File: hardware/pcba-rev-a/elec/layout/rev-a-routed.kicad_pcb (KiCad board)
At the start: 2 copper layers, 200 x 146 mm, 180 parts

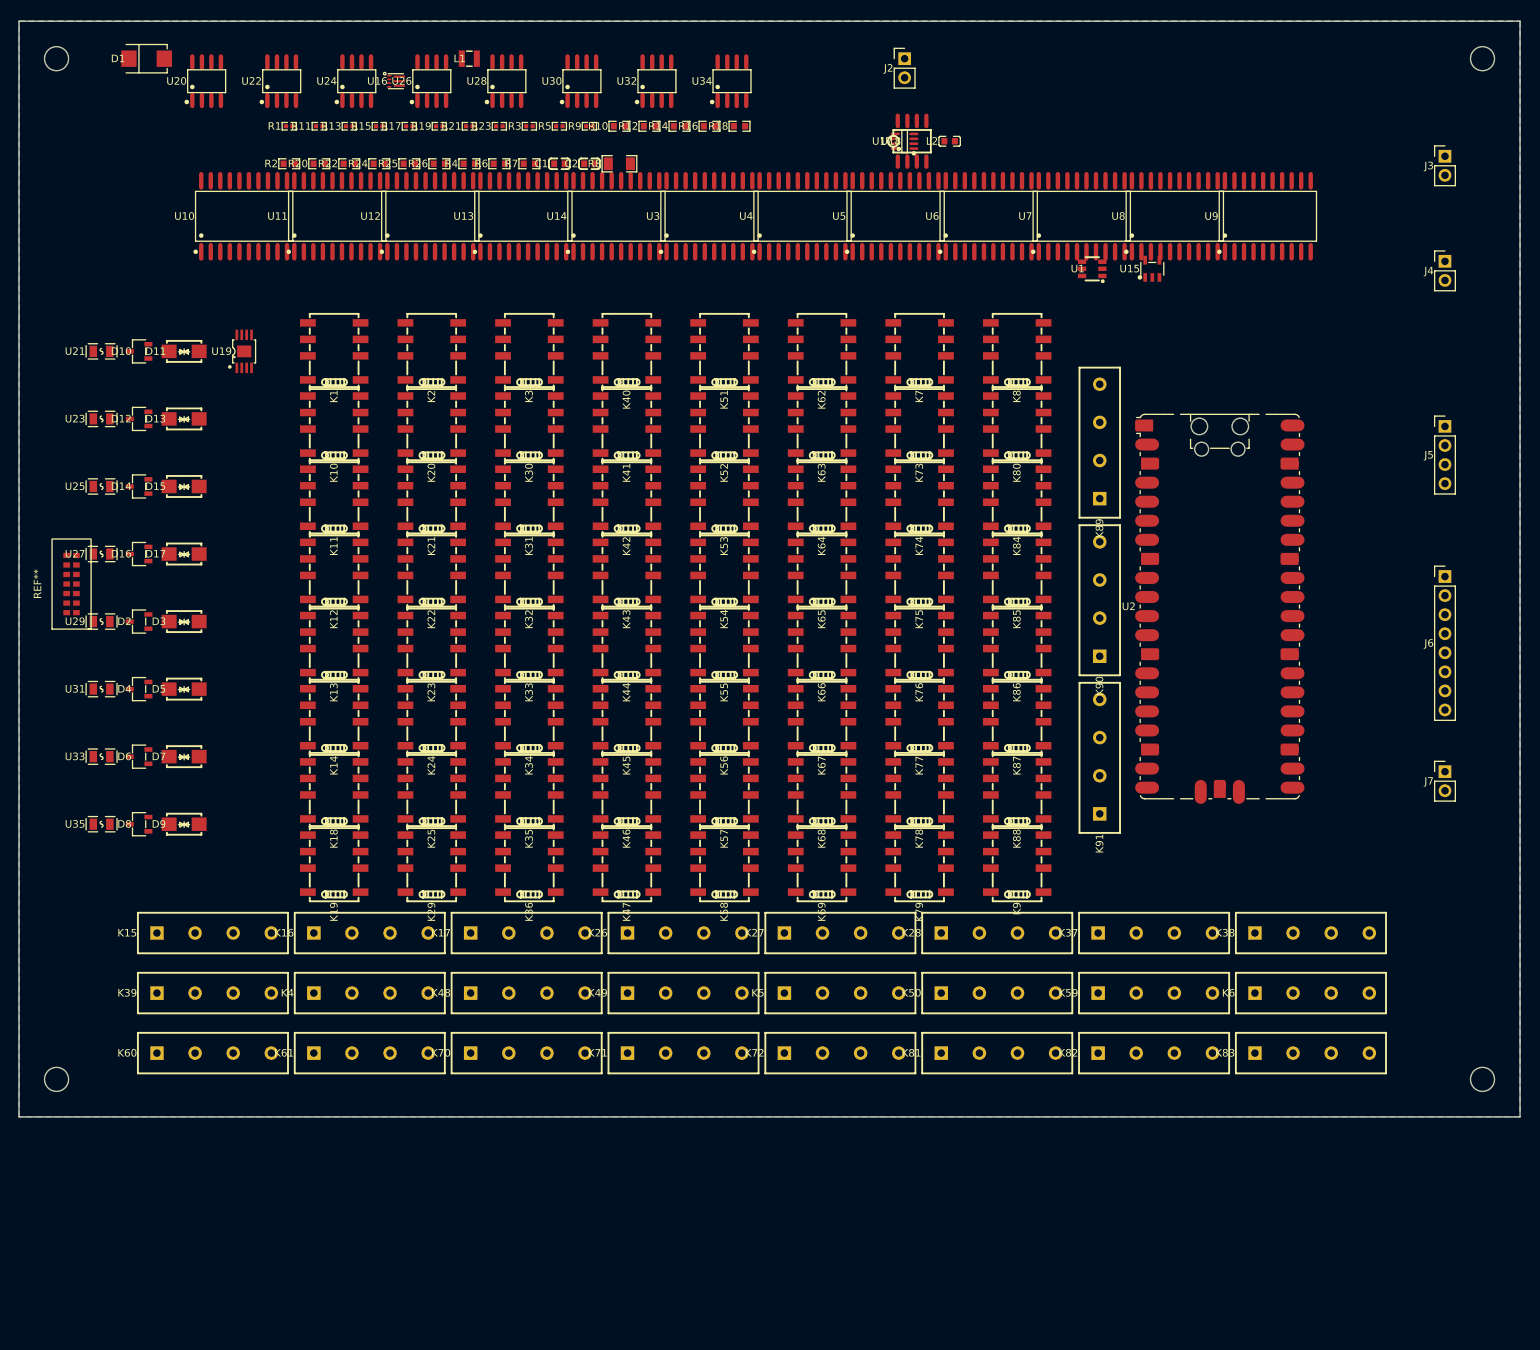
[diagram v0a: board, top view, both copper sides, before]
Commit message: Placement engine v3 + quality gates: kill the routing trial-and-error
Root cause of router struggles was connectivity-blind placement with
hardcoded pitches. Rebuilt as code we own and iterate:

- scripts/placement_score.py: pre-route GATE (courtyard overlaps,
  off-board) + HPWL score. Placements that fail never reach the router.
- Channel map v2 (LOCALITY): TPIC 1-8 each sink their own relay tree's
  8 G6K coils and sit directly above that tree; TPIC 9-11 sink the reed
  bank; TPIC 12 the reference block. 91 coil nets become short locals
  instead of cross-board runs. coil-channel-map.md updated (firmware
  shares the table).
- place_and_zone.py v3: pitches DERIVED from measured courtyards;
  relays grouped per tree by net classification (instance-path nets,
  sink aliases, drain-number decode -- the shared rail being named
  'sel_p4-coil_bus-hv' poisoned naive matching); TPICs placed by
  net-sharing vote with their relays; board grown to 200x175 from the
  measured vertical budget.
- Result: GATE PASS (was 12+ overlaps), HPWL 18862mm vs 20587 baseline.

freerouting stays the stock released jar (GPL source available, but the
placement was the lever, not the router).

Co-Authored-By: Claude Fable 5 <noreply@anthropic.com>
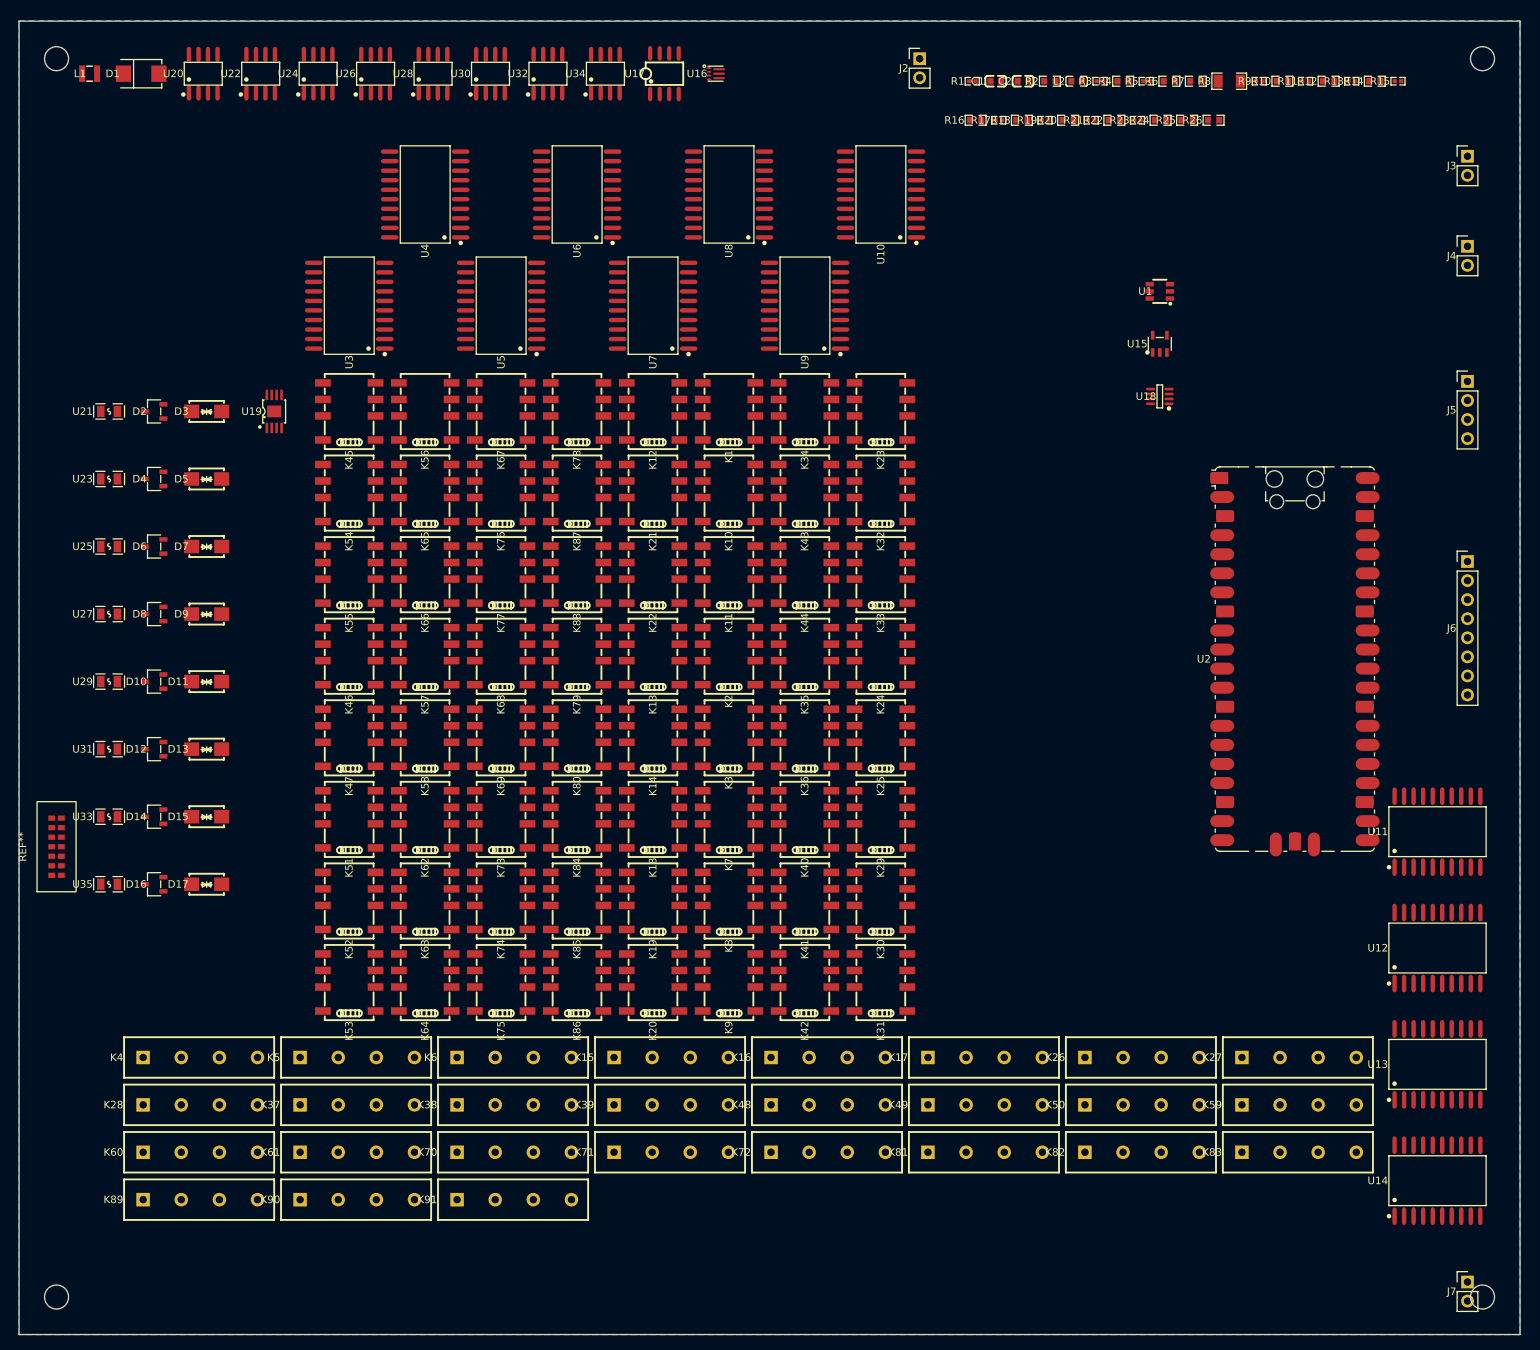
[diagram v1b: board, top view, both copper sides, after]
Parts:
- moved U14 168.8 mm to (229.0, 194.5)
- moved U11 168.0 mm to (229.0, 148.0)
- moved U13 166.1 mm to (229.0, 179.0)
- moved U12 165.9 mm to (229.0, 163.5)
- moved K89 156.7 mm to (64.2, 197.0), turned to 0 degrees
- moved R15 135.9 mm to (223.7, 48.0)
- moved R13 133.7 mm to (217.6, 48.0)
- moved R11 131.6 mm to (211.4, 48.0)
- moved K90 127.2 mm to (85.1, 197.0), turned to 0 degrees
- moved K28 108.8 mm to (64.2, 184.4)
- moved K37 108.8 mm to (85.1, 184.4)
- moved K38 108.8 mm to (106.0, 184.4)
- moved K6 106.7 mm to (106.0, 178.1)
- moved R24 104.3 mm to (192.1, 53.2)
- moved R25 103.8 mm to (195.6, 53.2)
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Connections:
- K13 pad 8: coil_n-13 -> coil_n-12
- K14 pad 8: coil_n-14 -> coil_n-13
- K18 pad 8: coil_n-16 -> coil_n-14
- K19 pad 8: coil_n-17 -> coil_n-15
- K2 pad 8: coil_n-18 -> coil_n-17
- K24 pad 8: coil_n-28 -> coil_n-27
- K25 pad 8: coil_n-29 -> coil_n-28
- K29 pad 8: coil_n-30 -> coil_n-29
- K3 pad 8: coil_n-20 -> coil_n-18
- K30 pad 8: coil_n-31 -> coil_n-30
- K35 pad 8: coil_n-24 -> coil_n-22
- K36 pad 8: coil_n-25 -> coil_n-23
- K40 pad 8: coil_n-26 -> coil_n-24
- K41 pad 8: coil_n-27 -> coil_n-25
- K46 pad 8: coil_n-11 -> coil_n-16
- K47 pad 8: coil_n-15 -> coil_n-21
- K51 pad 8: coil_n-19 -> coil_n-26
- K52 pad 8: coil_n-23 -> coil_n-31
- K7 pad 8: coil_n-21 -> coil_n-19
- K8 pad 8: coil_n-22 -> coil_n-20
- K85 pad 8: coil_n-12 -> coil_n-11
- U10 pad 14: coil_n-21 -> coil_n-28
- U10 pad 15: coil_n-22 -> coil_n-29
- U10 pad 16: sink_kfn_pwr -> coil_n-30
- U10 pad 17: sink_kfn_dmm_hi -> sink_ksn_pwr
- U10 pad 4: sink_kfn_scope_a -> sink_ksn_bank
- U10 pad 5: sink_kfn_scope_b -> sink_ksn_scope_a
- U10 pad 6: coil_n-18 -> sink_ksn_scope_b
- U10 pad 7: coil_n-20 -> coil_n-27
- U11 pad 14: sink_ksp_scope_b -> sink_p2_dmm_lo
- U11 pad 15: coil_n-24 -> sink_p2_gnd
- U11 pad 16: coil_n-25 -> sink_p3_dmm_hi
- U11 pad 17: coil_n-26 -> sink_p3_dmm_lo
- U11 pad 4: sink_kfn_dmm_lo -> sink_p1_dmm_hi
- U11 pad 5: sink_kfn_gnd -> sink_p1_dmm_lo
- U11 pad 6: sink_ksp_bank -> sink_p1_gnd
- U11 pad 7: sink_ksp_scope_a -> sink_p2_dmm_hi
- U12 pad 14: sink_ksp_gnd -> sink_kfp_dmm_hi
- U12 pad 15: sink_ksn_bank -> sink_kfp_dmm_lo
- U12 pad 16: sink_ksn_scope_a -> sink_kfp_gnd
- U12 pad 17: sink_ksn_scope_b -> sink_kfn_dmm_hi
- U12 pad 4: coil_n-27 -> sink_p3_gnd
- U12 pad 5: sink_ksp_pwr -> sink_p4_dmm_hi
- U12 pad 6: sink_ksp_dmm_hi -> sink_p4_dmm_lo
- U12 pad 7: sink_ksp_dmm_lo -> sink_p4_gnd
- U13 pad 14: sink_ksn_pwr -> sink_ksp_gnd
- U13 pad 4: coil_n-28 -> sink_kfn_dmm_lo
- U13 pad 5: coil_n-29 -> sink_kfn_gnd
- U13 pad 6: coil_n-30 -> sink_ksp_dmm_hi
- U13 pad 7: coil_n-31 -> sink_ksp_dmm_lo
- U3 pad 14: coil_n-15 -> coil_n-21
- U3 pad 15: coil_n-19 -> coil_n-26
- U3 pad 16: coil_n-23 -> coil_n-31
- U3 pad 7: coil_n-11 -> coil_n-16
- U4 pad 14: sink_p2_scope_a -> coil_n-1
- U4 pad 15: sink_p2_scope_b -> coil_n-2
- U4 pad 16: coil_n -> coil_n-3
- U4 pad 17: coil_n-1 -> sink_p2_pwr
- U4 pad 4: sink_p1_dmm_hi -> sink_p2_bank
- U4 pad 5: sink_p1_dmm_lo -> sink_p2_scope_a
- U4 pad 6: sink_p1_gnd -> sink_p2_scope_b
- U4 pad 7: sink_p2_bank -> coil_n
- U5 pad 14: sink_p2_dmm_lo -> coil_n-5
- U5 pad 15: sink_p2_gnd -> coil_n-6
- U5 pad 16: sink_p3_bank -> coil_n-7
- U5 pad 17: sink_p3_scope_a -> sink_p3_pwr
- U5 pad 4: coil_n-2 -> sink_p3_bank
- U5 pad 5: coil_n-3 -> sink_p3_scope_a
- U5 pad 6: sink_p2_pwr -> sink_p3_scope_b
- U5 pad 7: sink_p2_dmm_hi -> coil_n-4
- U6 pad 14: coil_n-7 -> coil_n-9
- U6 pad 15: sink_p3_pwr -> coil_n-10
- U6 pad 16: sink_p3_dmm_hi -> coil_n-11
- U6 pad 17: sink_p3_dmm_lo -> sink_p4_pwr
- U6 pad 4: sink_p3_scope_b -> sink_p4_bank
- U6 pad 5: coil_n-4 -> sink_p4_scope_a
- U6 pad 6: coil_n-5 -> sink_p4_scope_b
- U6 pad 7: coil_n-6 -> coil_n-8
- U7 pad 14: coil_n-8 -> coil_n-13
- U7 pad 15: coil_n-9 -> coil_n-14
- U7 pad 16: coil_n-10 -> coil_n-15
- U7 pad 17: coil_n-12 -> sink_kfp_pwr
- U7 pad 4: sink_p3_gnd -> sink_kfp_bank
- U7 pad 5: sink_p4_bank -> sink_kfp_scope_a
- U7 pad 6: sink_p4_scope_a -> sink_kfp_scope_b
- U7 pad 7: sink_p4_scope_b -> coil_n-12
- U8 pad 14: sink_kfp_bank -> coil_n-18
- U8 pad 15: sink_kfp_scope_a -> coil_n-19
- U8 pad 16: sink_kfp_scope_b -> coil_n-20
- U8 pad 17: coil_n-13 -> sink_kfn_pwr
- U8 pad 4: sink_p4_pwr -> sink_kfn_bank
- U8 pad 5: sink_p4_dmm_hi -> sink_kfn_scope_a
- U8 pad 6: sink_p4_dmm_lo -> sink_kfn_scope_b
- U8 pad 7: sink_p4_gnd -> coil_n-17
- U9 pad 14: sink_kfp_dmm_hi -> coil_n-23
- U9 pad 15: sink_kfp_dmm_lo -> coil_n-24
- U9 pad 16: sink_kfp_gnd -> coil_n-25
- U9 pad 17: sink_kfn_bank -> sink_ksp_pwr
- U9 pad 4: coil_n-14 -> sink_ksp_bank
- U9 pad 5: coil_n-16 -> sink_ksp_scope_a
- U9 pad 6: coil_n-17 -> sink_ksp_scope_b
- U9 pad 7: sink_kfp_pwr -> coil_n-22
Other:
- board size 200 x 146 mm -> 200 x 175 mm

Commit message: flroute v0: own Rust autorouter — DRC-clean copper, 35s vs 16min
Zero-dependency Rust crate replacing freerouting in the pipeline:
DSN in -> multi-source A* grid routing -> SES out (KiCad-importable).

Rev A benchmark: 145/174 nets (83%) in 35s with ZERO copper DRC
defects, vs freerouting's ~93% in ~16min WITH 7 defects. Remaining
nets: rip-up & reroute is the v1 feature; hybrid cleanup via
freerouting works today.

Correctness lessons baked in (each found by KiCad DRC as referee):
- grid pitch must derive from rules (width+clearance margin) or
  adjacent tracks violate by construction
- pad obstacles need continuous-coordinate rasterization (cell-snap
  shifted boxes up to half a pitch -> 20-90um clearance undershoots)
- per-pin (rotate) in DSN is load-bearing: dropping it swaps pad
  extents and produced every short on the board
- vias need a claimed neighborhood on all layers, not one cell
- KiCad's SES importer silently requires placement echo + library_out

Co-Authored-By: Claude Fable 5 <noreply@anthropic.com>
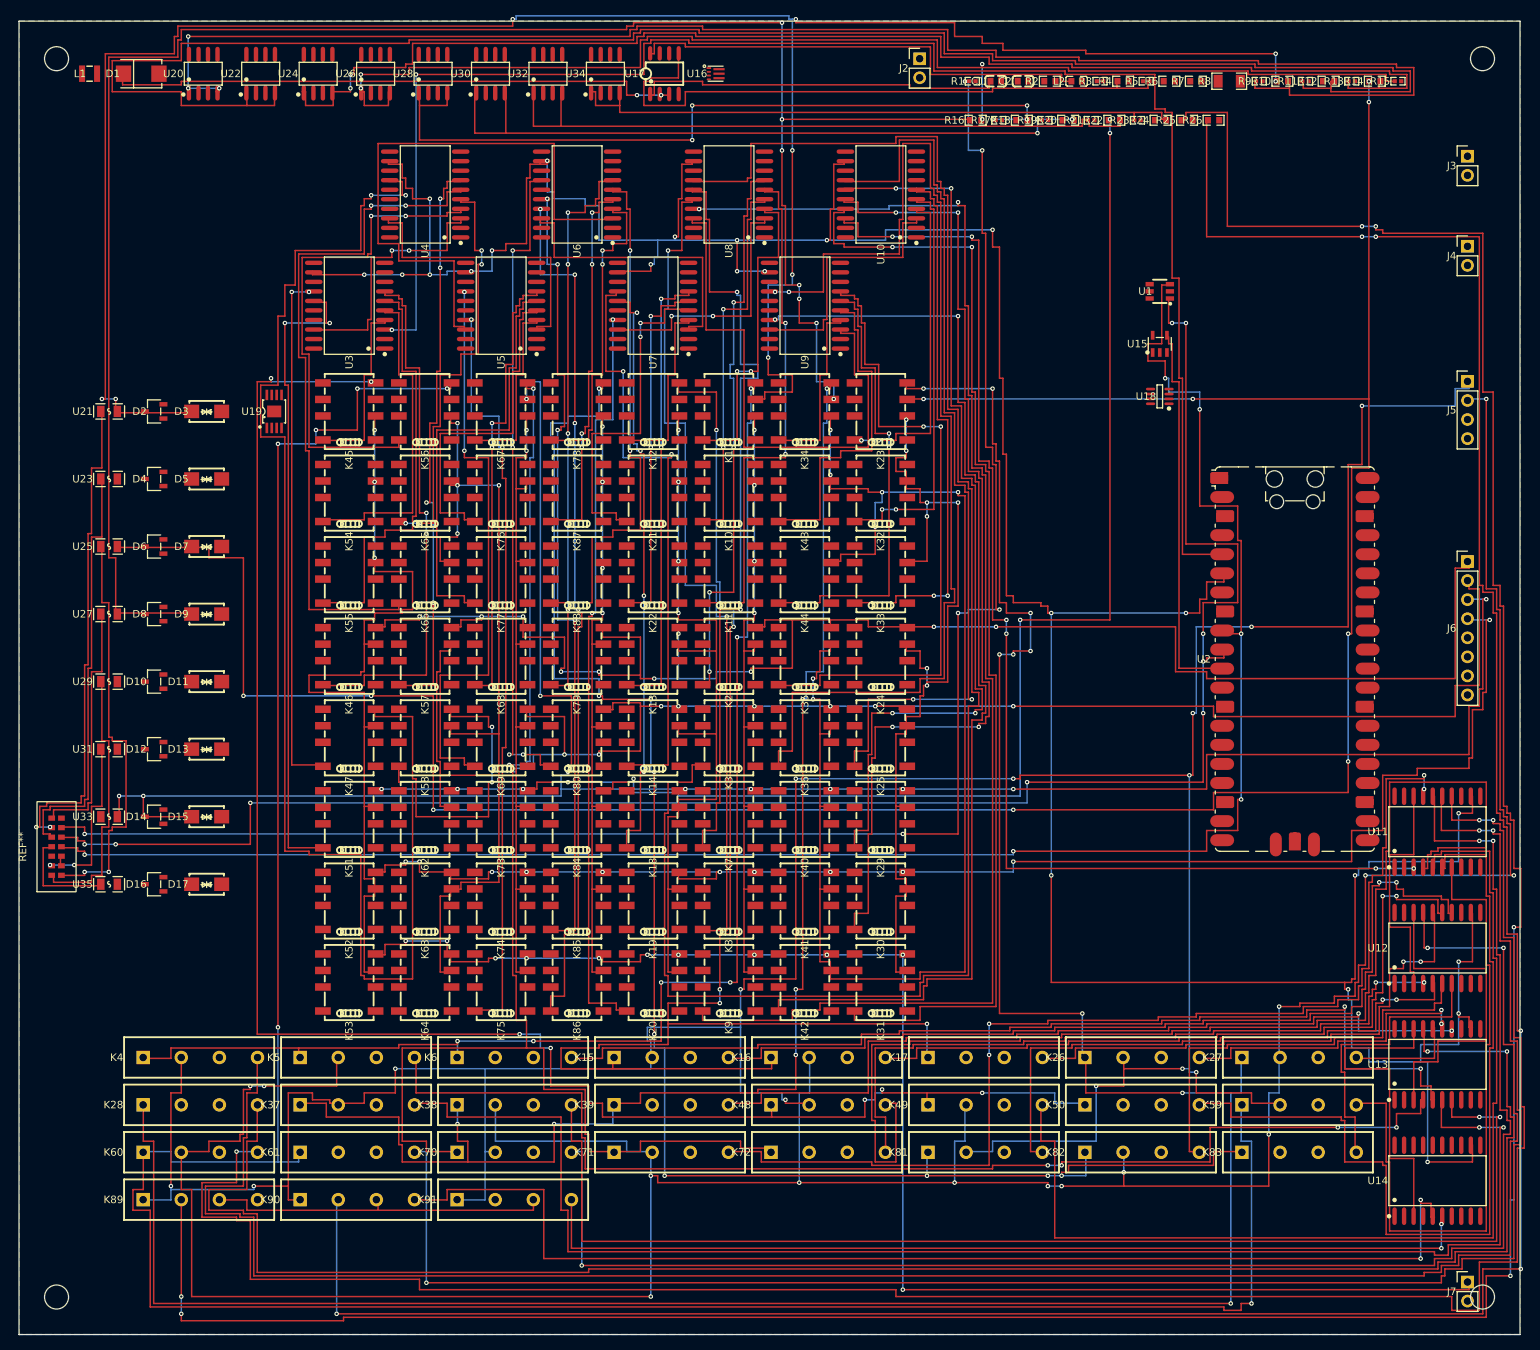
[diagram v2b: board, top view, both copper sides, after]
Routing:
- net RCK: track 0.00 -> 475.2 mm, vias 0 -> 23
- net dmm_hi: track 0.00 -> 451.3 mm, vias 0 -> 14
- net dmm_lo: track 0.00 -> 423.2 mm, vias 0 -> 14
- net refs-no-1: track 0.00 -> 401.6 mm, vias 0 -> 6
- net refs-no: track 0.00 -> 374.0 mm, vias 0 -> 5
- net node-2: track 0.00 -> 360.6 mm, vias 0 -> 10
- net matrix.sel_ksn-com-1: track 0.00 -> 351.9 mm, vias 0 -> 10
- net matrix.sel_p2-com-1: track 0.00 -> 351.0 mm, vias 0 -> 6
- net node-6: track 0.00 -> 300.4 mm, vias 0 -> 8
- net node: track 0.00 -> 292.1 mm, vias 0 -> 9
- net sink_p2_dmm_lo: track 0.00 -> 282.9 mm, vias 0 -> 3
- net sink_kfn_dmm_hi: track 0.00 -> 271.4 mm, vias 0 -> 2
- net node-3: track 0.00 -> 261.7 mm, vias 0 -> 7
- net sda: track 0.00 -> 252.1 mm, vias 0 -> 6
- net sink_ksn_gnd: track 0.00 -> 247.5 mm, vias 0 -> 2
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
